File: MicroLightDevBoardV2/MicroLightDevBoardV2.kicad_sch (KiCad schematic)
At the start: 58 parts, among them J1 Conn_01x05_Socket, J10 Conn_01x01_Socket, J11 Conn_01x04_Socket, J12 Conn_01x05_Socket, J13 Conn_01x02_Socket, J14 Conn_01x04_Socket, J15 Conn_01x04_Socket, J16 Conn_01x05_Socket, J17 Conn_01x01_Socket, J18 Conn_01x03_Socket, J19 Conn_01x03_Socket, J2 Conn_01x05_Socket, J20 Conn_01x02_Socket, J21 Conn_01x02_Socket, J22 Conn_01x02_Socket, J23 Conn_01x02_Socket, J24 Conn_01x01_Socket, J25 Conn_01x06_Socket, J26 Conn_01x04_Socket, J3 Conn_01x05_Socket, J4 Conn_01x05_Socket, J5 Conn_01x02_Socket, J6 Conn_01x02_Socket, J7 TYPE-C-31-M-12, J8 Conn_01x02_Socket, J9 Conn_01x02_Socket, U1 BQ25628RYKR, U2 ATtiny3226-M, U3 S-85S1AB33-I6T1U, U4 USBLC6-2P6, U5 MC3479

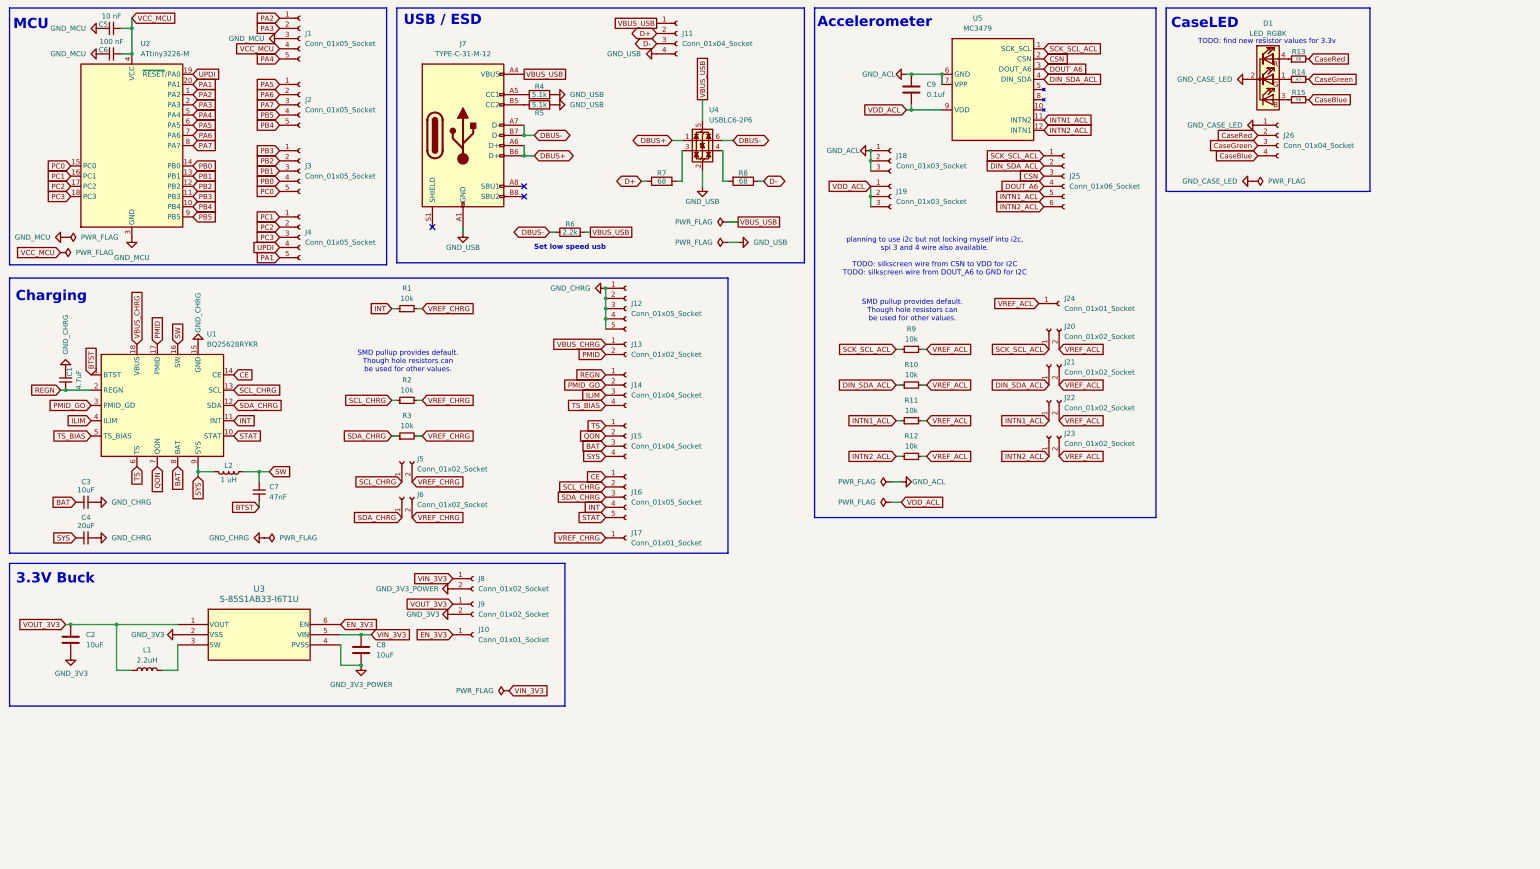
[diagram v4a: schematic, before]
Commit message: add power lanes
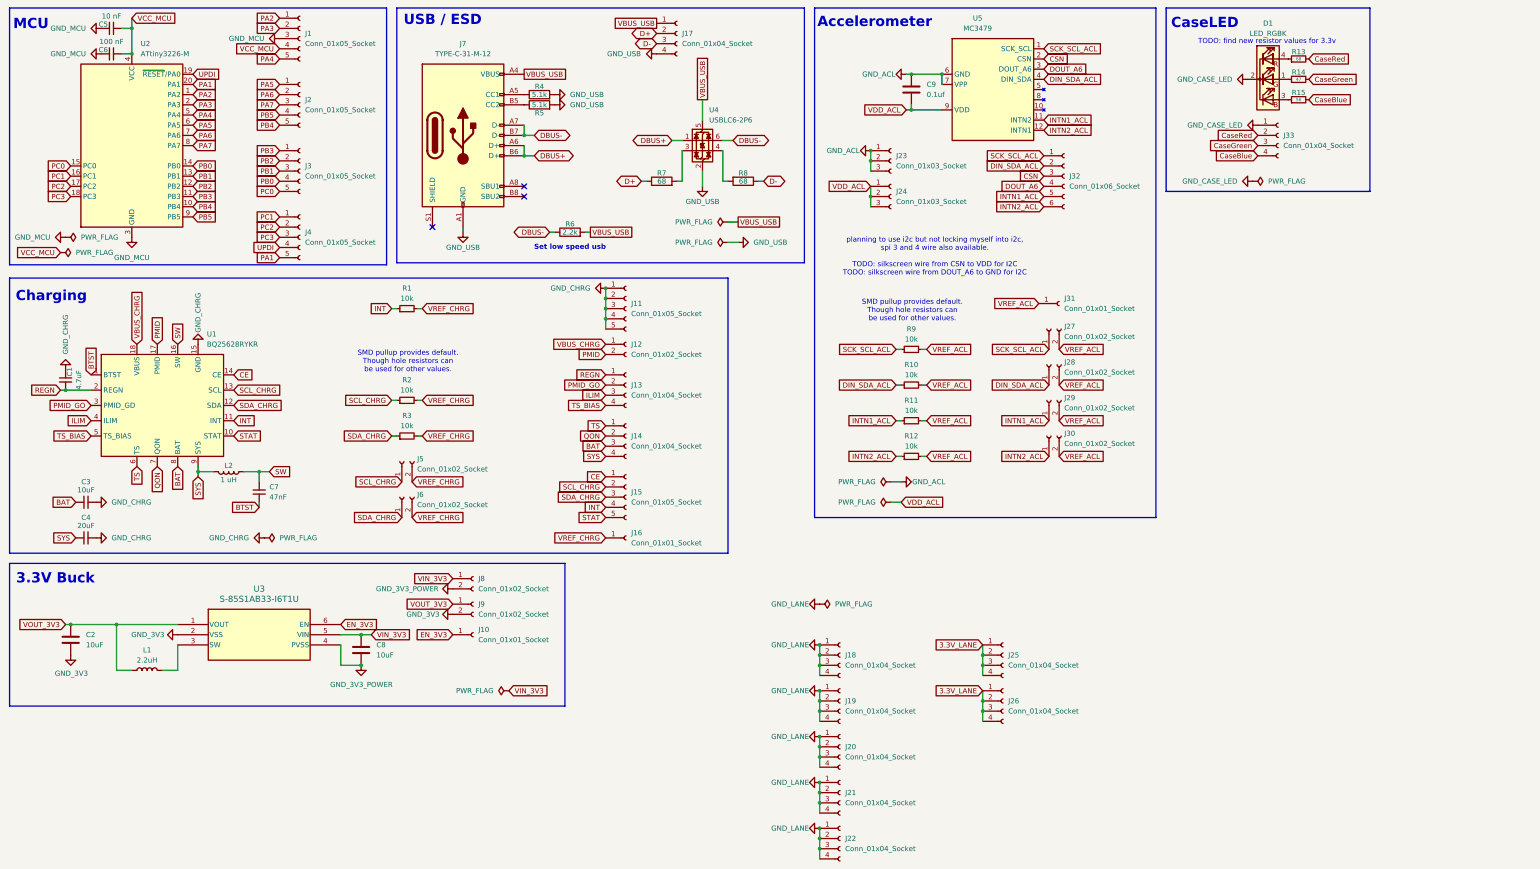
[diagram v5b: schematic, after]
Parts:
- added J18, J19, J20, J21, J22, J25, J26: Conn_01x04_Socket, Connector_PinHeader_2.54mm:PinHeader_1x04_P2.54mm_Vertical, symbol Connector:Conn_01x04_Socket
- renumbered J12 to J11, J13 to J12, J14 to J13, J15 to J14, J16 to J15, J17 to J16, J11 to J17, J18 to J23, J19 to J24, J20 to J27, J21 to J28, J22 to J29, J23 to J30, J24 to J31, J25 to J32, J26 to J33
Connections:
- new net 3.3V_LANE: J25.1 (Pin_1), J25.2 (Pin_2), J25.3 (Pin_3), J25.4 (Pin_4), J26.1 (Pin_1), J26.2 (Pin_2), J26.3 (Pin_3), J26.4 (Pin_4)
- new net GND_LANE: J18.1 (Pin_1), J18.2 (Pin_2), J18.3 (Pin_3), J18.4 (Pin_4), J19.1 (Pin_1), J19.2 (Pin_2), J19.3 (Pin_3), J19.4 (Pin_4), J20.1 (Pin_1), J20.2 (Pin_2), J20.3 (Pin_3), J20.4 (Pin_4), J21.1 (Pin_1), J21.2 (Pin_2), J21.3 (Pin_3), J21.4 (Pin_4), J22.1 (Pin_1), J22.2 (Pin_2), J22.3 (Pin_3), J22.4 (Pin_4)

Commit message: fix pin socket footprints
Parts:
- J1, J11, J15, J2, J3, J4: footprint Connector_PinHeader_2.54mm:PinHeader_1x05_P2.54mm_Vertical -> Connector_PinSocket_2.54mm:PinSocket_1x05_P2.54mm_Vertical
- J10, J16, J31: footprint Connector_PinHeader_2.54mm:PinHeader_1x01_P2.54mm_Vertical -> Connector_PinSocket_2.54mm:PinSocket_1x01_P2.54mm_Vertical
- J12, J27, J28, J29, J30, J5, J6, J8, J9: footprint Connector_PinHeader_2.54mm:PinHeader_1x02_P2.54mm_Vertical -> Connector_PinSocket_2.54mm:PinSocket_1x02_P2.54mm_Vertical
- J13, J14, J17, J18, J19, J20, J21, J22, J25, J26, J33: footprint Connector_PinHeader_2.54mm:PinHeader_1x04_P2.54mm_Vertical -> Connector_PinSocket_2.54mm:PinSocket_1x04_P2.54mm_Vertical
- J23, J24: footprint Connector_PinHeader_2.54mm:PinHeader_1x03_P2.54mm_Vertical -> Connector_PinSocket_2.54mm:PinSocket_1x03_P2.54mm_Vertical
- J32: footprint Connector_PinHeader_2.54mm:PinHeader_1x06_P2.54mm_Vertical -> Connector_PinSocket_2.54mm:PinSocket_1x06_P2.54mm_Vertical
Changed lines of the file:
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@@
 			)
 		)
-		(property "Footprint" "Connector_PinHeader_2.54mm:PinHeader_1x02_P2.54mm_Vertical"
+		(property "Footprint" "Connector_PinSocket_2.54mm:PinSocket_1x02_P2.54mm_Vertical"
 			(at 274.32 104.14 0)
 			(effects
@@
 			)
 		)
-		(property "Footprint" "Connector_PinHeader_2.54mm:PinHeader_1x02_P2.54mm_Vertical"
+		(property "Footprint" "Connector_PinSocket_2.54mm:PinSocket_1x02_P2.54mm_Vertical"
 			(at 274.32 121.92 0)
 			(effects
@@
 			)
 		)
-		(property "Footprint" "Connector_PinHeader_2.54mm:PinHeader_1x04_P2.54mm_Vertical"
+		(property "Footprint" "Connector_PinSocket_2.54mm:PinSocket_1x04_P2.54mm_Vertical"
 			(at 168.91 121.92 0)
 			(effects
@@
 			)
 		)
-		(property "Footprint" "Connector_PinHeader_2.54mm:PinHeader_1x02_P2.54mm_Vertical"
+		(property "Footprint" "Connector_PinSocket_2.54mm:PinSocket_1x02_P2.54mm_Vertical"
 			(at 113.03 128.27 0)
 			(effects
@@
 			)
 		)
-		(property "Footprint" "Connector_PinHeader_2.54mm:PinHeader_1x05_P2.54mm_Vertical"
+		(property "Footprint" "Connector_PinSocket_2.54mm:PinSocket_1x05_P2.54mm_Vertical"
 			(at 87.63 72.39 0)
 			(effects
@@
 			)
 		)
-		(property "Footprint" "Connector_PinHeader_2.54mm:PinHeader_1x02_P2.54mm_Vertical"
+		(property "Footprint" "Connector_PinSocket_2.54mm:PinSocket_1x02_P2.54mm_Vertical"
 			(at 130.81 163.83 0)
 			(effects
@@
 			)
 		)
-		(property "Footprint" "Connector_PinHeader_2.54mm:PinHeader_1x02_P2.54mm_Vertical"
+		(property "Footprint" "Connector_PinSocket_2.54mm:PinSocket_1x02_P2.54mm_Vertical"
 			(at 274.32 113.03 0)
 			(effects
@@
 			)
 		)
-		(property "Footprint" "Connector_PinHeader_2.54mm:PinHeader_1x04_P2.54mm_Vertical"
+		(property "Footprint" "Connector_PinSocket_2.54mm:PinSocket_1x04_P2.54mm_Vertical"
 			(at 222.25 222.25 0)
 			(effects
@@
 			)
 		)
-		(property "Footprint" "Connector_PinHeader_2.54mm:PinHeader_1x01_P2.54mm_Vertical"
+		(property "Footprint" "Connector_PinSocket_2.54mm:PinSocket_1x01_P2.54mm_Vertical"
 			(at 130.81 171.45 0)
 			(effects
@@
 			)
 		)
-		(property "Footprint" "Connector_PinHeader_2.54mm:PinHeader_1x01_P2.54mm_Vertical"
+		(property "Footprint" "Connector_PinSocket_2.54mm:PinSocket_1x01_P2.54mm_Vertical"
 			(at 276.86 88.9 0)
 			(effects
@@
 			)
 		)
-		(property "Footprint" "Connector_PinHeader_2.54mm:PinHeader_1x04_P2.54mm_Vertical"
+		(property "Footprint" "Connector_PinSocket_2.54mm:PinSocket_1x04_P2.54mm_Vertical"
 			(at 181.61 21.59 0)
 			(effects
@@
 			)
 		)
-		(property "Footprint" "Connector_PinHeader_2.54mm:PinHeader_1x02_P2.54mm_Vertical"
+		(property "Footprint" "Connector_PinSocket_2.54mm:PinSocket_1x02_P2.54mm_Vertical"
 			(at 274.32 95.25 0)
 			(effects
@@
 			)
 		)
-		(property "Footprint" "Connector_PinHeader_2.54mm:PinHeader_1x03_P2.54mm_Vertical"
+		(property "Footprint" "Connector_PinSocket_2.54mm:PinSocket_1x03_P2.54mm_Vertical"
 			(at 234.95 62.23 0)
 			(effects
@@
 			)
 		)
-		(property "Footprint" "Connector_PinHeader_2.54mm:PinHeader_1x05_P2.54mm_Vertical"
+		(property "Footprint" "Connector_PinSocket_2.54mm:PinSocket_1x05_P2.54mm_Vertical"
 			(at 168.91 90.17 0)
 			(effects
@@
 			)
 		)
-		(property "Footprint" "Connector_PinHeader_2.54mm:PinHeader_1x04_P2.54mm_Vertical"
+		(property "Footprint" "Connector_PinSocket_2.54mm:PinSocket_1x04_P2.54mm_Vertical"
 			(at 168.91 109.22 0)
 			(effects
@@
 			)
 		)
-		(property "Footprint" "Connector_PinHeader_2.54mm:PinHeader_1x05_P2.54mm_Vertical"
+		(property "Footprint" "Connector_PinSocket_2.54mm:PinSocket_1x05_P2.54mm_Vertical"
 			(at 87.63 39.37 0)
 			(effects
@@
 			)
 		)
-		(property "Footprint" "Connector_PinHeader_2.54mm:PinHeader_1x04_P2.54mm_Vertical"
+		(property "Footprint" "Connector_PinSocket_2.54mm:PinSocket_1x04_P2.54mm_Vertical"
 			(at 222.25 176.53 0)
 			(effects
@@
 			)
 		)
-		(property "Footprint" "Connector_PinHeader_2.54mm:PinHeader_1x04_P2.54mm_Vertical"
+		(property "Footprint" "Connector_PinSocket_2.54mm:PinSocket_1x04_P2.54mm_Vertical"
 			(at 222.25 210.82 0)
 			(effects
@@
 			)
 		)
-		(property "Footprint" "Connector_PinHeader_2.54mm:PinHeader_1x02_P2.54mm_Vertical"
+		(property "Footprint" "Connector_PinSocket_2.54mm:PinSocket_1x02_P2.54mm_Vertical"
 			(at 130.81 157.48 0)
 			(effects
@@
 			)
 		)
-		(property "Footprint" "Connector_PinHeader_2.54mm:PinHeader_1x06_P2.54mm_Vertical"
+		(property "Footprint" "Connector_PinSocket_2.54mm:PinSocket_1x06_P2.54mm_Vertical"
 			(at 278.13 57.15 0)
 			(effects
@@
 			)
 		)
-		(property "Footprint" "Connector_PinHeader_2.54mm:PinHeader_1x02_P2.54mm_Vertical"
+		(property "Footprint" "Connector_PinSocket_2.54mm:PinSocket_1x02_P2.54mm_Vertical"
 			(at 113.03 137.16 0)
 			(effects
@@
 			)
 		)
-		(property "Footprint" "Connector_PinHeader_2.54mm:PinHeader_1x04_P2.54mm_Vertical"
+		(property "Footprint" "Connector_PinSocket_2.54mm:PinSocket_1x04_P2.54mm_Vertical"
 			(at 222.25 199.39 0)
 			(effects
@@
 			)
 		)
-		(property "Footprint" "Connector_PinHeader_2.54mm:PinHeader_1x04_P2.54mm_Vertical"
+		(property "Footprint" "Connector_PinSocket_2.54mm:PinSocket_1x04_P2.54mm_Vertical"
 			(at 262.89 187.96 0)
 			(effects
@@
 			)
 		)
-		(property "Footprint" "Connector_PinHeader_2.54mm:PinHeader_1x05_P2.54mm_Vertical"
+		(property "Footprint" "Connector_PinSocket_2.54mm:PinSocket_1x05_P2.54mm_Vertical"
 			(at 168.91 137.16 0)
 			(effects
@@
 			)
 		)
-		(property "Footprint" "Connector_PinHeader_2.54mm:PinHeader_1x05_P2.54mm_Vertical"
+		(property "Footprint" "Connector_PinSocket_2.54mm:PinSocket_1x05_P2.54mm_Vertical"
 			(at 87.63 22.86 0)
 			(effects
@@
 			)
 		)
-		(property "Footprint" "Connector_PinHeader_2.54mm:PinHeader_1x01_P2.54mm_Vertical"
+		(property "Footprint" "Connector_PinSocket_2.54mm:PinSocket_1x01_P2.54mm_Vertical"
 			(at 168.91 147.32 0)
 			(effects
@@
 			)
 		)
-		(property "Footprint" "Connector_PinHeader_2.54mm:PinHeader_1x04_P2.54mm_Vertical"
+		(property "Footprint" "Connector_PinSocket_2.54mm:PinSocket_1x04_P2.54mm_Vertical"
 			(at 222.25 187.96 0)
 			(effects
@@
 			)
 		)
-		(property "Footprint" "Connector_PinHeader_2.54mm:PinHeader_1x05_P2.54mm_Vertical"
+		(property "Footprint" "Connector_PinSocket_2.54mm:PinSocket_1x05_P2.54mm_Vertical"
 			(at 87.63 55.88 0)
 			(effects
@@
 			)
 		)
-		(property "Footprint" "Connector_PinHeader_2.54mm:PinHeader_1x04_P2.54mm_Vertical"
+		(property "Footprint" "Connector_PinSocket_2.54mm:PinSocket_1x04_P2.54mm_Vertical"
 			(at 331.47 46.99 0)
 			(effects
@@
 			)
 		)
-		(property "Footprint" "Connector_PinHeader_2.54mm:PinHeader_1x03_P2.54mm_Vertical"
+		(property "Footprint" "Connector_PinSocket_2.54mm:PinSocket_1x03_P2.54mm_Vertical"
 			(at 234.95 53.34 0)
 			(effects
@@
 			)
 		)
-		(property "Footprint" "Connector_PinHeader_2.54mm:PinHeader_1x02_P2.54mm_Vertical"
+		(property "Footprint" "Connector_PinSocket_2.54mm:PinSocket_1x02_P2.54mm_Vertical"
 			(at 168.91 99.06 0)
 			(effects
@@
 			)
 		)
-		(property "Footprint" "Connector_PinHeader_2.54mm:PinHeader_1x04_P2.54mm_Vertical"
+		(property "Footprint" "Connector_PinSocket_2.54mm:PinSocket_1x04_P2.54mm_Vertical"
 			(at 262.89 176.53 0)
 			(effects

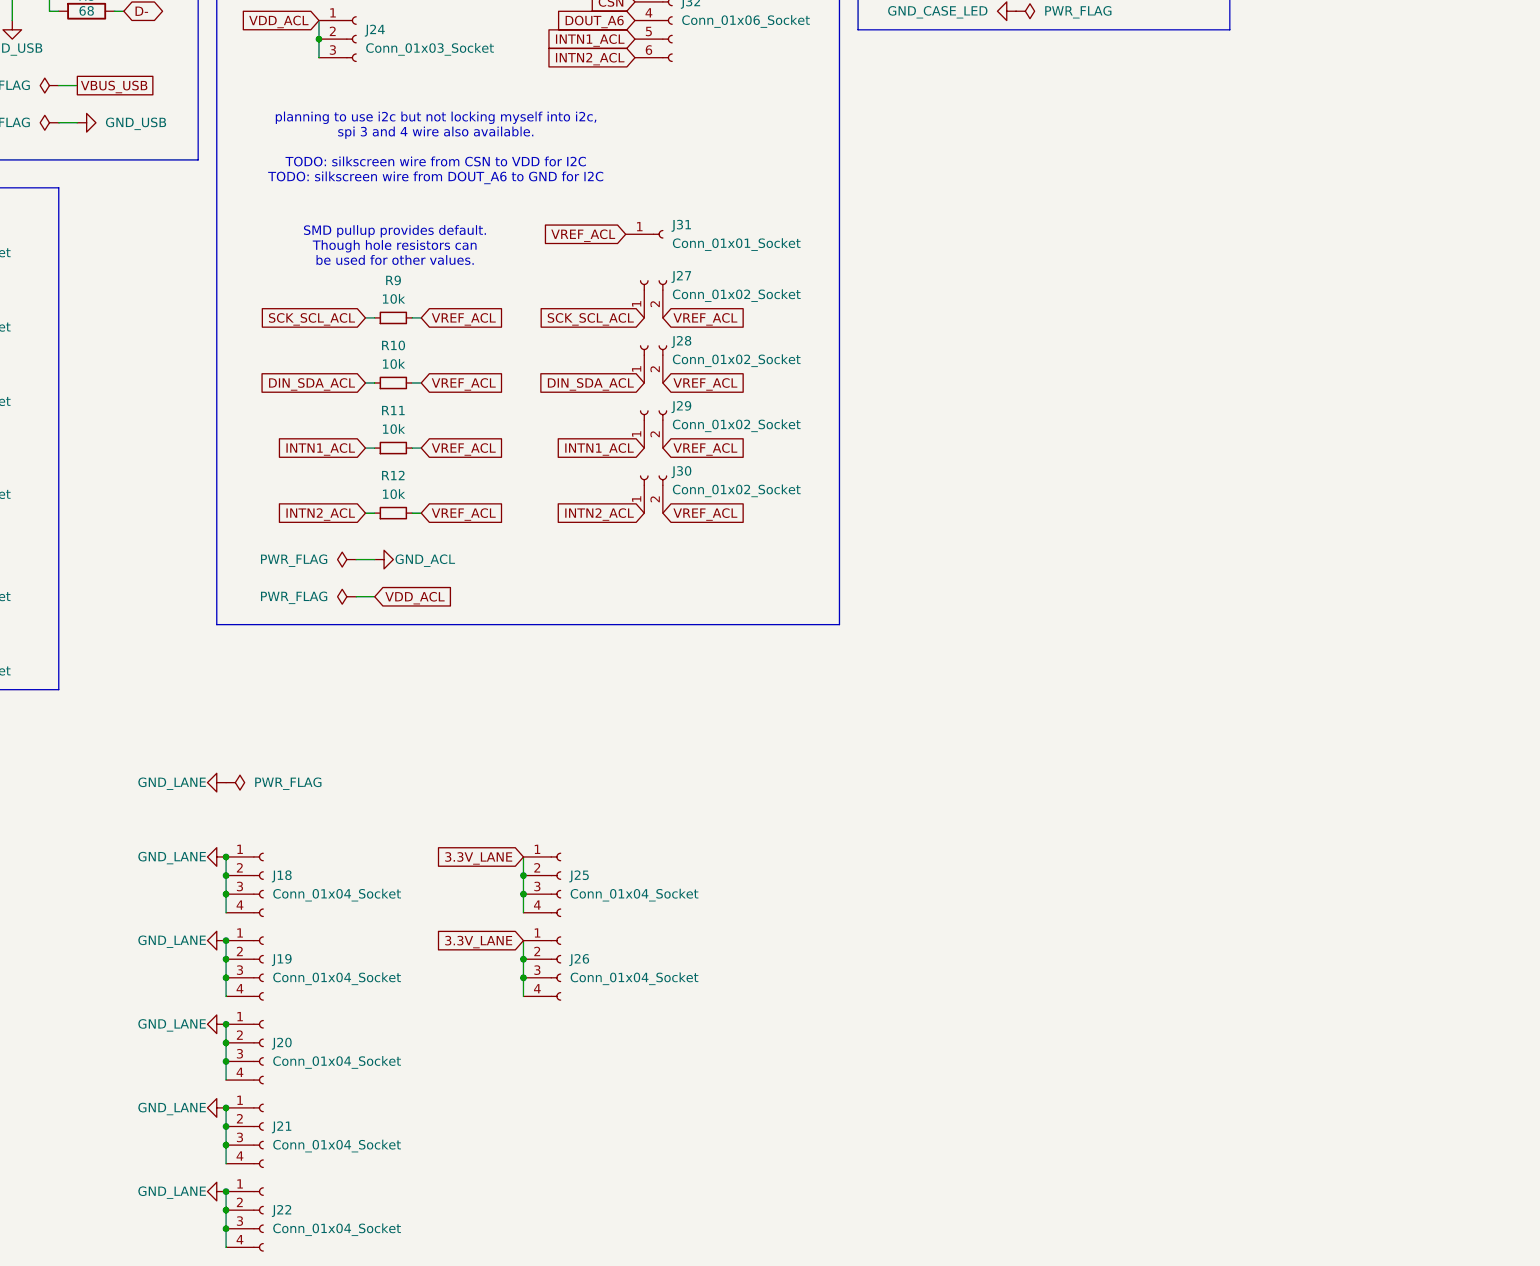
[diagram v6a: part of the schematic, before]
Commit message: added pin labels to silk screen
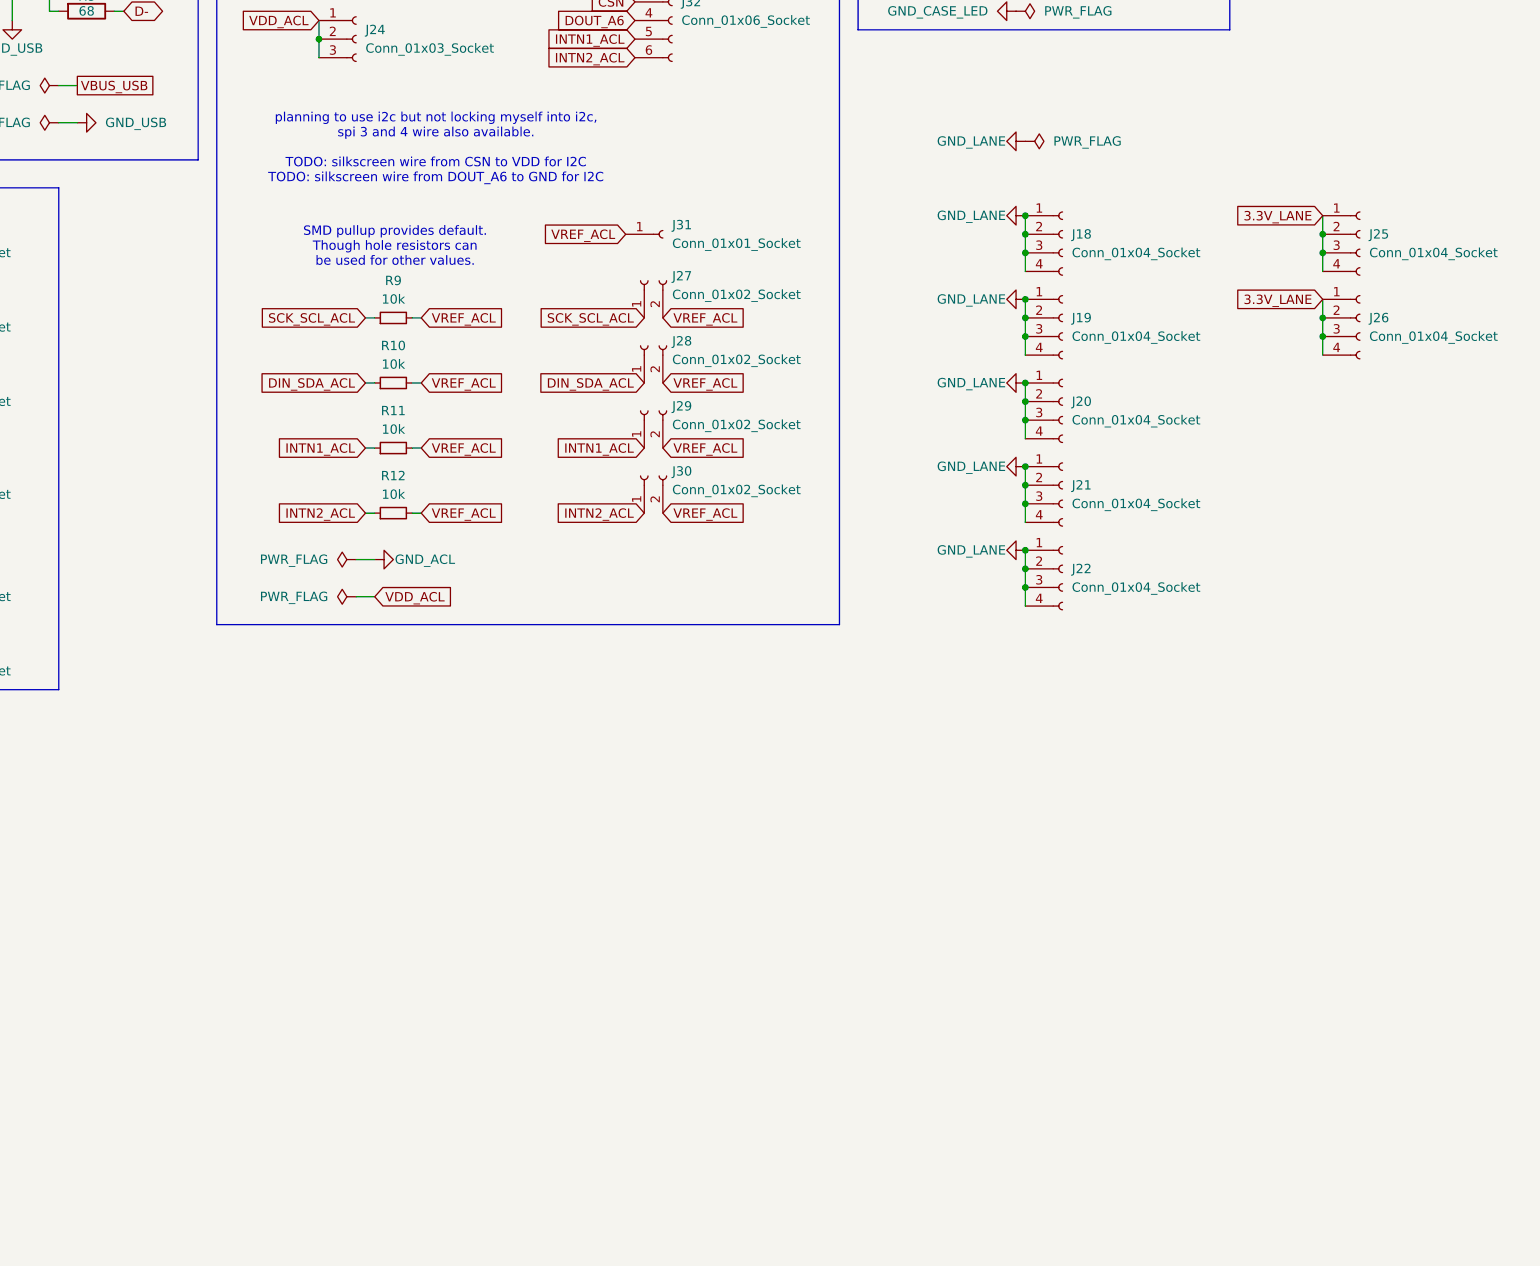
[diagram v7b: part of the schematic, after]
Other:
- moved on the sheet: J18, J19, J20, J21, J22, J25, J26
